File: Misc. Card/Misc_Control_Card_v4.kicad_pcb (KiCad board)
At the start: 2 copper layers, 99.9 x 62 mm, 58 parts, among them IC2_P1 Conn_01x02, IC2_P2 Conn_01x02, IC2_P3 Conn_01x02, J1 Conn_01x03_Pin, J2 Conn_01x02, J4 Conn_01x02, J5 Conn_01x02, J7 Screw_Terminal_01x02, J8 Conn_01x03, J9 Conn_01x03_Pin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

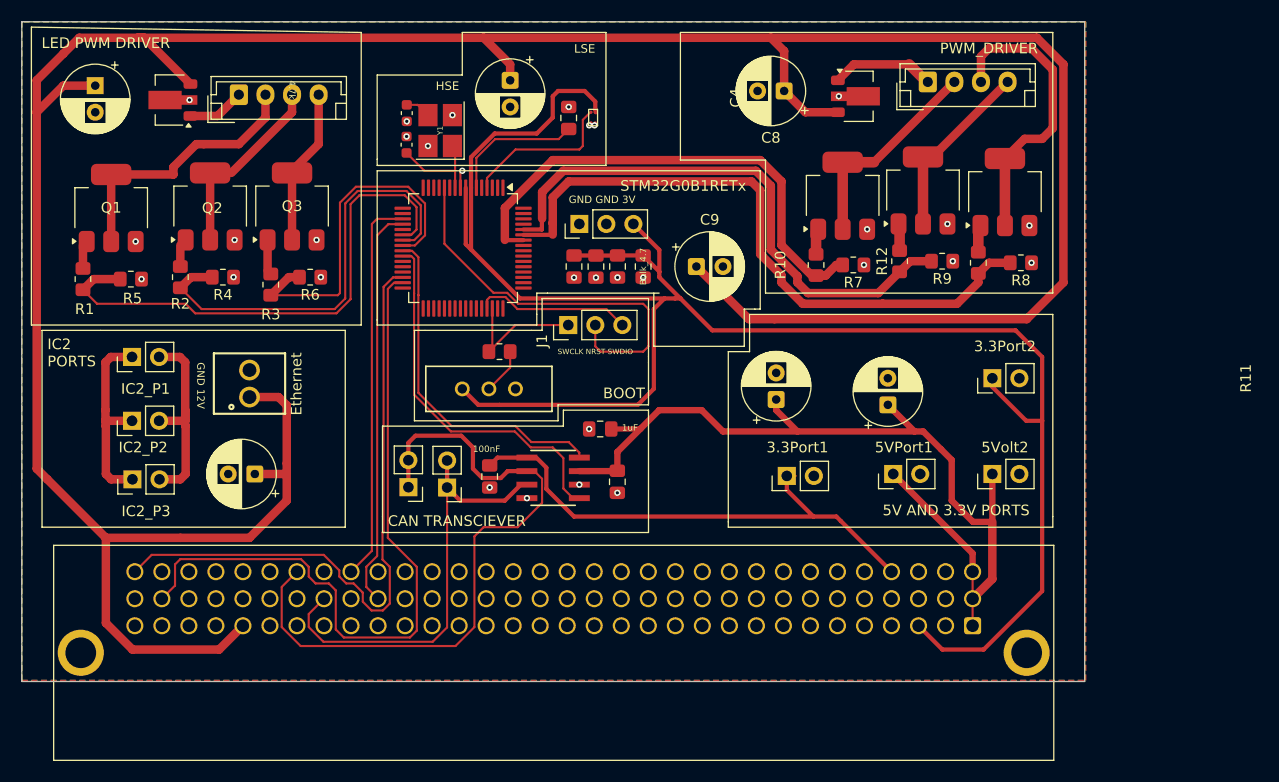
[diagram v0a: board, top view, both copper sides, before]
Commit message: Added CAN Impedance Matching
Misc Card
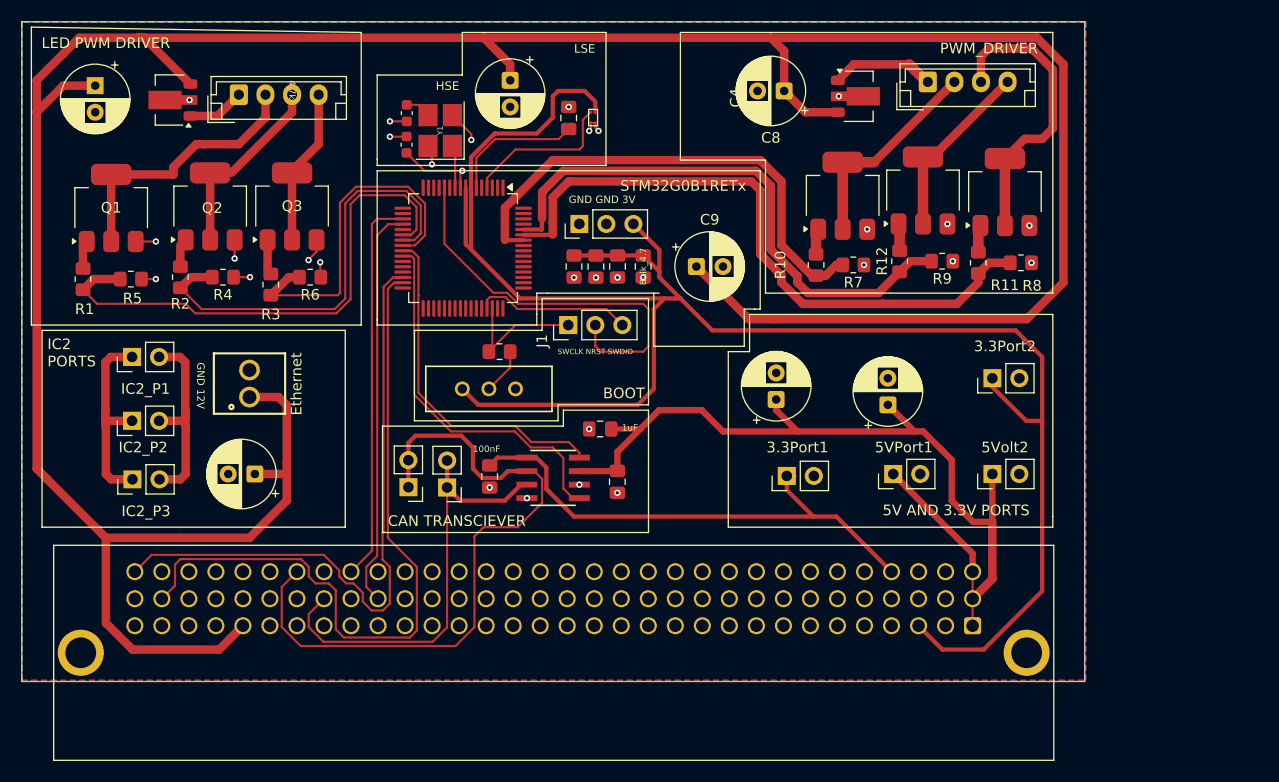
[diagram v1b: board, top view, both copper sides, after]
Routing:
- net GND: track 1.67 -> 22.1 mm
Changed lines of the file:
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@@
 		(tags "resistor handsolder")
 		(property "Reference" "R8"
-			(at 0 -1.65 0)
+			(at -1.05 -2.15 0)
 			(layer "F.SilkS")
 			(effects
@@
 		(tags "resistor handsolder")
 		(property "Reference" "R11"
-			(at -10.85 25.15 90)
+			(at -2.1 2.5 180)
 			(layer "F.SilkS")
 			(effects
@@
 	)
 	(segment
+		(start 178.15 72.95)
+		(end 178.2 73)
+		(width 0.2)
+		(layer "F.Cu")
+		(net 1)
+	)
+	(segment
+		(start 177.05 71.35)
+		(end 177.8 70.6)
+		(width 0.2)
+		(layer "F.Cu")
+		(net 1)
+	)
+	(segment
+		(start 171.55 73)
+		(end 170 73)
+		(width 0.2)
+		(layer "F.Cu")
+		(net 1)
+	)
+	(segment
+		(start 203.59 58.5)
+		(end 203.59 59.0866)
+		(width 0.2)
+		(layer "F.Cu")
+		(net 1)
+	)
+	(segment
+		(start 192.35 59.5476)
+		(end 190.5724 57.77)
+		(width 0.2)
+		(layer "F.Cu")
+		(net 1)
+	)
+	(segment
+		(start 203.59 59.0866)
+		(end 203.4266 59.25)
+		(width 0.2)
+		(layer "F.Cu")
+		(net 1)
+	)
+	(segment
+		(start 203.59 58.5)
+		(end 204 58.5)
+		(width 0.2)
+		(layer "F.Cu")
+		(net 1)
+	)
+	(segment
+		(start 184.7 59.8)
+		(end 186.2374 59.8)
+		(width 0.2)
+		(layer "F.Cu")
+		(net 1)
+	)
+	(segment
+		(start 162.7 69.65)
+		(end 160.8 69.65)
+		(width 0.2)
+		(layer "F.Cu")
+		(net 1)
+	)
+	(segment
+		(start 188.65 61.0476)
+		(end 188.2724 60.67)
+		(width 0.2)
+		(layer "F.Cu")
+		(net 1)
+	)
+	(segment
+		(start 192.35 60.1)
+		(end 192.35 59.5476)
+		(width 0.2)
+		(layer "F.Cu")
+		(net 1)
+	)
+	(segment
+		(start 170.1 71.25)
+		(end 170.1 69.5)
+		(width 0.2)
+		(layer "F.Cu")
+		(net 1)
+	)
+	(segment
+		(start 188.65 62.4)
+		(end 188.65 61.0476)
+		(width 0.2)
+		(layer "F.Cu")
+		(net 1)
+	)
+	(segment
+		(start 184.7 58.355)
+		(end 186.2824 58.355)
+		(width 0.2)
+		(layer "F.Cu")
+		(net 1)
+	)
+	(segment
 		(start 191.3224 63.1776)
 		(end 191.5 63)
@@
 		(net 1)
 	)
+	(segment
+		(start 177.8 70.6)
+		(end 177.8 69.5)
+		(width 0.2)
+		(layer "F.Cu")
+		(net 1)
+	)
+	(segment
+		(start 178.15 71.6)
+		(end 178.15 72.95)
+		(width 0.2)
+		(layer "F.Cu")
+		(net 1)
+	)
+	(segment
+		(start 177.05 71.4)
+		(end 177.05 71.35)
+		(width 0.2)
+		(layer "F.Cu")
+		(net 1)
+	)
+	(segment
+		(start 186.2374 59.8)
+		(end 186.2624 59.775)
+		(width 0.2)
+		(layer "F.Cu")
+		(net 1)
+	)
+	(segment
+		(start 162.7 73.182379)
+		(end 161.35 73.182379)
+		(width 0.2)
+		(layer "F.Cu")
+		(net 1)
+	)
+	(segment
+		(start 204 58.95)
+		(end 204 58.5)
+		(width 0.2)
+		(layer "F.Cu")
+		(net 1)
+	)
+	(segment
+		(start 204.3 59.25)
+		(end 204 58.95)
+		(width 0.2)
+		(layer "F.Cu")
+		(net 1)
+	)
 	(via
 		(at 226.8875 56)
@@
 	)
 	(via
-		(at 170.1 69.5)
+		(at 170.1 71.25)
 		(size 0.6)
 		(drill 0.3)
@@
 	)
 	(via
-		(at 177.8 69.5)
+		(at 177.05 71.4)
 		(size 0.6)
 		(drill 0.3)
@@
 	)
 	(via
-		(at 170 73)
+		(at 171.55 73)
 		(size 0.6)
 		(drill 0.3)
@@
 	)
 	(via
-		(at 203.9276 58.73)
+		(at 204.3 59.25)
 		(size 0.6)
 		(drill 0.3)
@@
 	)
 	(via
-		(at 203.4276 58.73)
+		(at 203.4266 59.25)
 		(size 0.6)
 		(drill 0.3)
@@
 	)
 	(via
-		(at 160.8 69.65)
+		(at 162.7 69.65)
 		(size 0.6)
 		(drill 0.3)
@@
 	)
 	(via
-		(at 161.35 73.182379)
+		(at 162.7 73.182379)
 		(size 0.6)
 		(drill 0.3)
@@
 	)
 	(via
-		(at 188.2724 60.67)
+		(at 188.65 62.4)
 		(size 0.6)
 		(drill 0.3)
@@
 	)
 	(via
-		(at 186.2824 58.355)
+		(at 184.7 58.355)
 		(size 0.6)
 		(drill 0.3)
@@
 	)
 	(via
-		(at 178.2 73)
+		(at 178.15 71.6)
 		(size 0.6)
 		(drill 0.3)
@@
 	)
 	(via
-		(at 186.2624 59.775)
+		(at 184.7 59.8)
 		(size 0.6)
 		(drill 0.3)
@@
 	)
 	(via
-		(at 190.5724 57.77)
+		(at 192.35 60.1)
 		(size 0.6)
 		(drill 0.3)
